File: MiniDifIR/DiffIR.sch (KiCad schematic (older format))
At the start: 17 parts, among them IC1 ATTINY25-SS, P1 AVR_ISP, P2 OUT

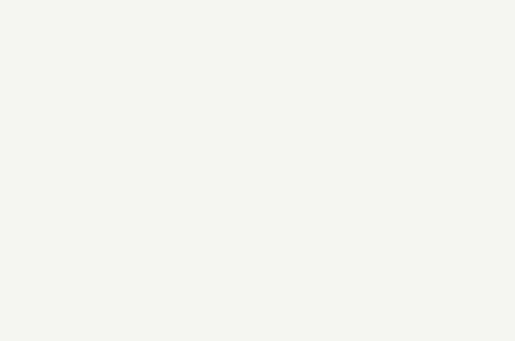
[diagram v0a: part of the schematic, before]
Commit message: thickened traces
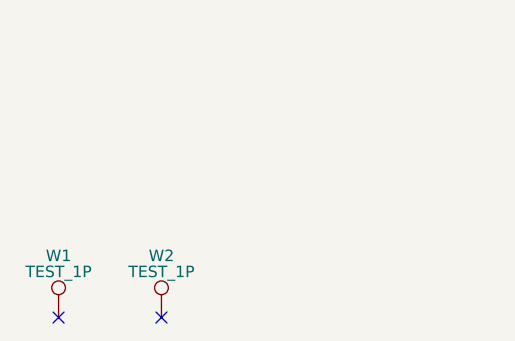
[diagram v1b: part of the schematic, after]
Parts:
- added W1, W2: TEST_1P, Mounting_Holes:MountingHole_3mm, symbol TEST_1P
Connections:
- no-connect marks 0 -> 2
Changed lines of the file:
@@
 LIBS:graphic
 LIBS:xilinx
+LIBS:DiffIR-cache
 EELAYER 25 0
 EELAYER END
@@
 Wire Wire Line
 	2575 2400 2575 3425
+$Comp
+L TEST_1P W1
+U 1 1 56F6ED18
+P 2275 5375
+F 0 "W1" H 2275 5645 50  0000 C CNN
+F 1 "TEST_1P" H 2275 5575 50  0000 C CNN
+F 2 "Mounting_Holes:MountingHole_3mm" H 2475 5375 50  0001 C CNN
+F 3 "" H 2475 5375 50  0000 C CNN
+	1    2275 5375
+	1    0    0    -1
+$EndComp
+$Comp
+L TEST_1P W2
+U 1 1 56F6ED5F
+P 2725 5375
+F 0 "W2" H 2725 5645 50  0000 C CNN
+F 1 "TEST_1P" H 2725 5575 50  0000 C CNN
+F 2 "Mounting_Holes:MountingHole_3mm" H 2925 5375 50  0001 C CNN
+F 3 "" H 2925 5375 50  0000 C CNN
+	1    2725 5375
+	1    0    0    -1
+$EndComp
+NoConn ~ 2725 5375
+NoConn ~ 2275 5375
 $EndSCHEMATC
